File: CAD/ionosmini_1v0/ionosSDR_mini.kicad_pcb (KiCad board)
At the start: 4 copper layers, 168 x 80 mm, 63 parts, among them CON1 TFC-120-02-F-D-A-K-TR, CON2 TFC-120-02-F-D-A-K-TR, IC1 ESP32-S3-DEVKITC-1-N8R2, SW1 PTS647SK38SMTR2 LFS, SW2 PTS647SK38SMTR2 LFS, SW3 PTS647SK38SMTR2 LFS, SW4 PTS647SK38SMTR2 LFS, SW5 BACK, SW6 OK, U1 LP5907MFX-3.3

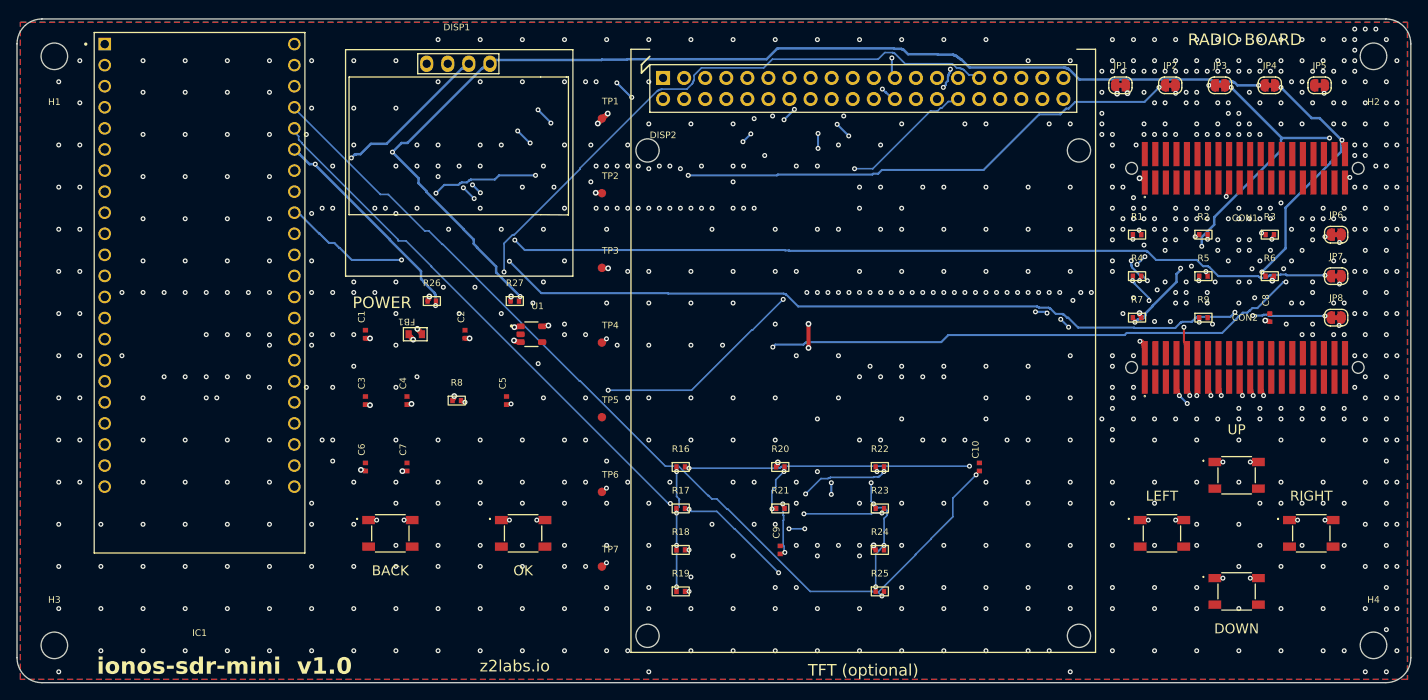
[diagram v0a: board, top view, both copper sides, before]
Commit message: rev-B3 PCB: pin map v2 parts, full re-route with 0/45/90 deg tracks
New parts placed: C11/C12 at the TFT VDD pin, R28-R32 header pull-ups
in a row under the display socket, R33 (NA 0R) and TP8 next to the
radio board sockets, R34 and the optional SW7 SPARE key.

All tracks and vias ripped and re-routed in three layer-role passes
(power on In2, the FG23 / TFT buses on In1, the rest on In1 and B.Cu;
F.Cu stays GND with pad fan-out only). Octilinear only: 0 % any-angle
segments, staircases straightened (1092 -> 970 segments), then GND
stitching on the new geometry (1394 vias, every GND island tied).

Silkscreen to JLCPCB rules (silk-to-pad 0.15 mm, line 0.15 mm, text
1.0/0.15 mm); references that sat on pads or on another part's silk
moved, FB1 turned upright, TP8 label pulled in from the board edge.
lib_footprint_mismatch warnings are expected: the board copies of
those footprints carry the trimmed silk.

TFC-120-02-F-D-A STEP replaced with the current Samtec model (same
geometry, AP214, coloured contacts); twin 3D reference images
recaptured, key still at the pin 1 end. DISP1 3D offset corrected.
twin_3d registers each 3D model's pins against its pads (steppins.py).

DRC 0 errors, 0 unconnected, schematic parity 0. README: buttons and
ladders, VRF_IN / 5V_RADIO, display and touch section, DevKit clone vs
official board note, new 3D render.
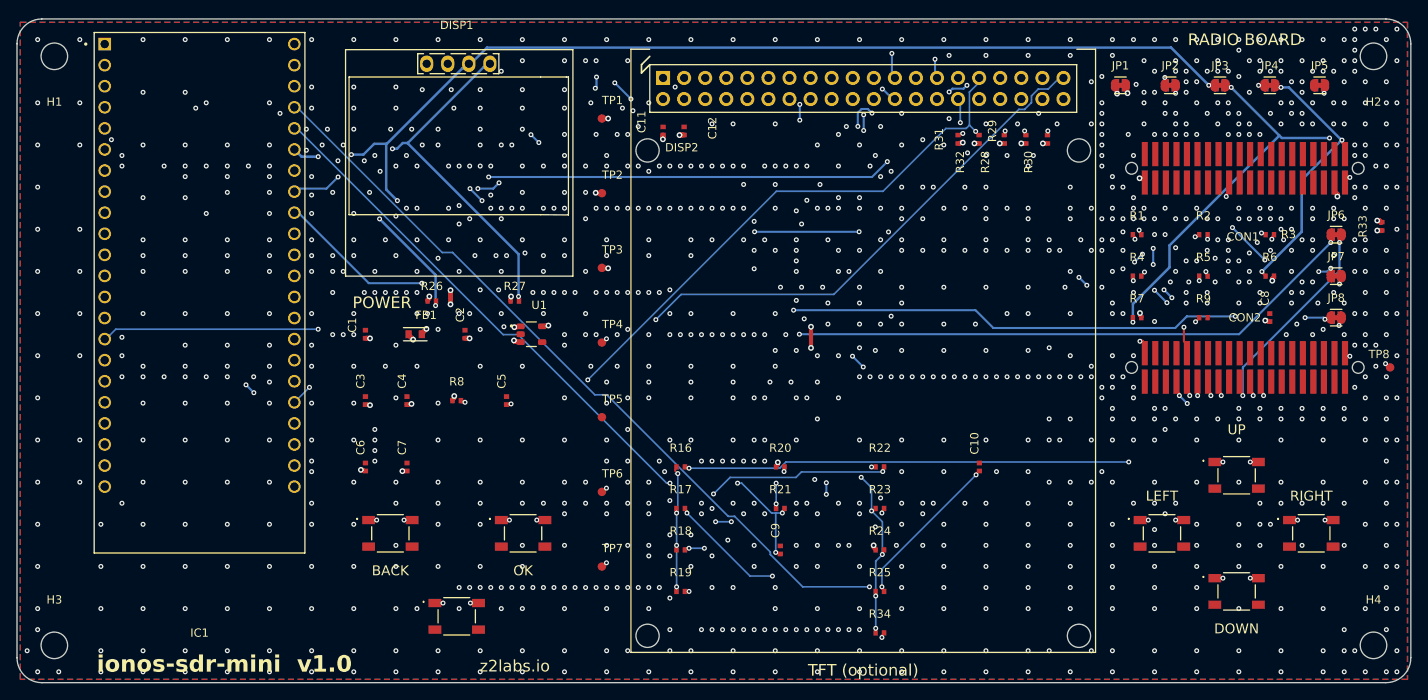
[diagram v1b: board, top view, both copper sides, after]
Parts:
- added C11: 10uF/6.3V, rpw_lib:CAPC1005X60_0402, F.Cu at (127.9, 63.5)
- added C12: 100nF/50V/10%, rpw_lib:CAPC1005X60_0402, F.Cu at (130.4, 63.5)
- added R28: 10k, rpw_lib:RESC1005X40_0402, F.Cu at (169.0, 64.5)
- added R29: 10k, rpw_lib:RESC1005X40_0402, F.Cu at (171.6, 64.5)
- added R30: 10k, rpw_lib:RESC1005X40_0402, F.Cu at (174.2, 64.5)
- added R31: 4.7k, rpw_lib:RESC1005X40_0402, F.Cu at (163.4, 64.5)
- added R32: 4.7k, rpw_lib:RESC1005X40_0402, F.Cu at (166.0, 64.5)
- added R33: NA(0R), rpw_lib:RESC1005X40_0402, F.Cu at (214.5, 75.0)
- added R34: 6.8k/1%, rpw_lib:RESC1005X40_0402, F.Cu at (154.0, 124.0)
- added SW7: NA(PTS647SK38), rpw_lib:PTS647SK38SMTR2LFS, F.Cu at (103.0, 122.0)
- added TP8: VRF_IN, rpw_lib:TESTPOINT_40MIL_SMD, F.Cu at (215.5, 92.0)
- C1, C6: value 10u -> 10uF/6.3V
- C10, C4, C5, C7, C8, C9: value 100n -> 100nF/50V/10%
- C2, C3: value 1u -> 1uF/16V/10%
- JP1, JP2, JP3, JP4, JP5, JP6, JP7, JP8: value ~ -> Bridged
- R17, R23: value 2k2 -> 2.2k/1%
- R18: value 6k8 -> 6.8k/1%
- R19: value 22k -> 22k/1%
- R20, R24: value 10k -> 10k/1%
- R26, R27: value 4k7 DNP -> NA(4.7k)
- SW5: value BACK -> PTS647SK38SMTR2 LFS
- SW6: value OK -> PTS647SK38SMTR2 LFS
- U1: value LP5907MFX-3.3 -> LP5907MFX-3.3(SOT23-5)
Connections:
- CON1 pad 37: unconnected-(CON1-Pad37) -> 5V_RADIO
- CON2 pad 40: unconnected-(CON2-Pad40) -> VRF_IN
- DISP2 pad 35: unconnected-(DISP2-SD_/CS-Pad35) -> SD_CS
- DISP2 pad 36: unconnected-(DISP2-FONT_/CS-Pad36) -> FONT_CS
- DISP2 pad 37: unconnected-(DISP2-FLASH_/CS-Pad37) -> FLASH_CS
- IC1 pad J1_15: TCH_B -> TCH_INT
- IC1 pad J3_18: TCH_INT -> TCH_B
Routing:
- net 5V0: track 98.6 -> 206.7 mm, vias 4 -> 8
- net BTN_A3: track 0.00 -> 57.2 mm, vias 0 -> 3
- net TCH_B: track 123.4 -> 103.1 mm, vias 1 -> 3
- net TCH_INT: track 109.2 -> 129.1 mm
- net 5V_RADIO: track 0.00 -> 8.46 mm, vias 0 -> 2
- net SD_CS: track 0.00 -> 7.73 mm, vias 0 -> 1
- net FLASH_CS: track 0.00 -> 7.63 mm, vias 0 -> 1
- net VRF_IN: track 0.00 -> 6.16 mm, vias 0 -> 2
- net BTN_A_RAW: track 18.4 -> 24.2 mm, vias 5 -> 6
- net TFT_CS: track 103.6 -> 109.4 mm, vias 1 -> 3
- net FONT_CS: track 0.00 -> 4.57 mm, vias 0 -> 1
- net TCH_A: track 111.6 -> 115.4 mm, vias 1 -> 2
- net FG23_CMD: track 98.1 -> 101.1 mm, vias 6 -> 7
- net TFT_DC: track 105.6 -> 107.2 mm, vias 2 -> 4
- net SWDIO: track 127.3 -> 128.8 mm, vias 2 -> 6
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
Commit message: PCB: stitch every GND pour pocket, centre tracks in their channels
The zone filler drops pieces of GND pour that have no connection
(island removal), so a strip of GND between two tracks with no via in
it was simply missing - white holes all over the 2-layer F.Cu. Every
such pocket now gets a via into connected GND on another layer
(0.45/0.3 mm where the 0.6/0.3 via does not fit), and the next fill
keeps it. What is left is narrower than a via, or has no connected
GND on any other layer to tie to (e.g. between the TFT header rows).

Straight runs that pass between obstacles on both sides (a track
between two header pins) are moved to the middle of the channel; the
neighbouring segments stay on their own lines, so the routing stays
0/45/90 deg.

DRC 0 errors, 0 unconnected, schematic parity 0; twin unchanged.
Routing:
- net 3V3_RADIO: track 171.4 -> 172.9 mm
- net TFT_SCK: track 116.2 -> 117.2 mm
- net FG23_RDY: track 95.5 -> 96.4 mm
- net TCH_INT: track 129.1 -> 129.8 mm
- net TFT_DC: track 107.2 -> 107.9 mm
- net TFT_CS: track 109.4 -> 109.9 mm
- net FG23_SPARE_RB: track 51.4 -> 51.9 mm
- net GND: vias 1193 -> 1283

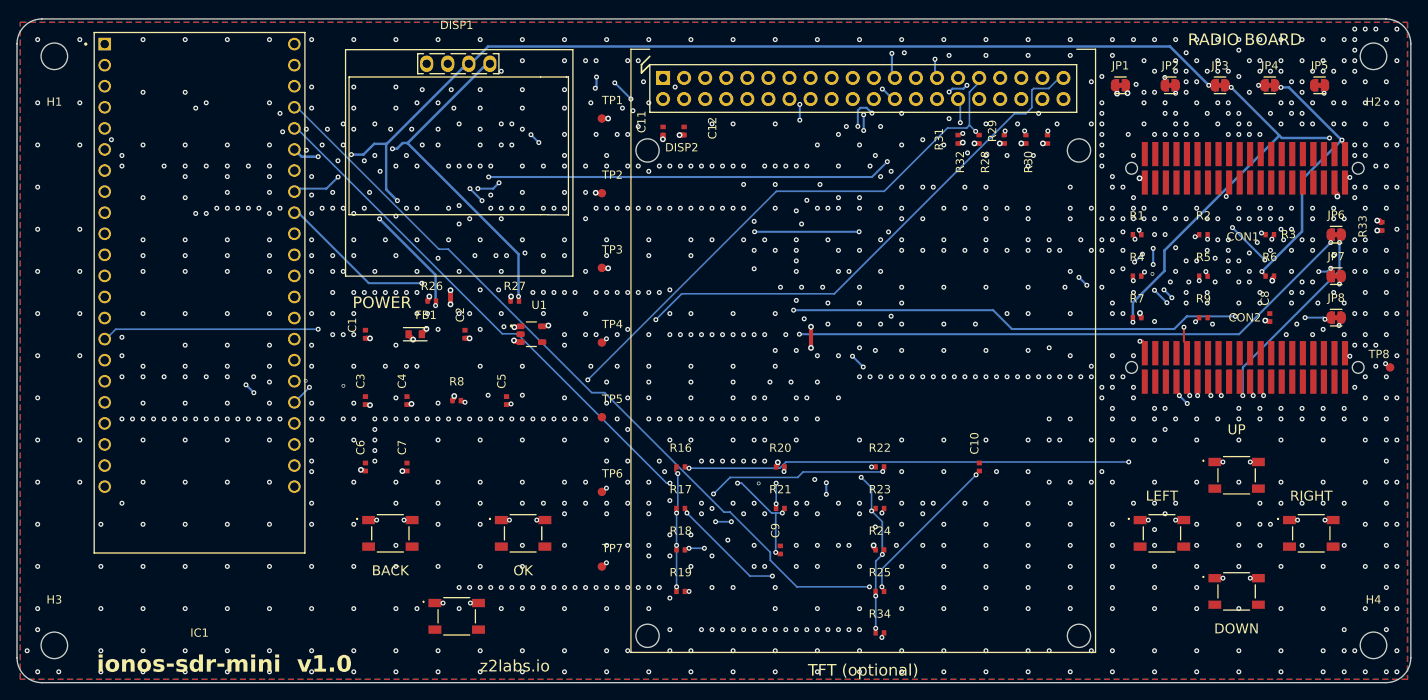
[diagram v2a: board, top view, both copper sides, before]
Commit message: SWD debug header CON3 (1x6 2.54 mm, not fitted) for an external debugger
Flashing the FG23 so far went only through the ESP32's bit-banged SWD.
CON3 adds a row of six plated holes on the right board edge, outside
the radio board's outline, for a J-Link / Simplicity Link with a pogo
clip or solder-in pins. Pin order follows the Tag-Connect TC2030-CTX:
1 VTref (VMCU_IN), 2 SWDIO, 3 nRESET, 4 SWCLK, 5 GND, 6 SWO.

The pins are on the radio side of the solder-jumper cut points
(SWDIO_RB, SWCLK_RB, SWO_RB, RESETn_RB): with JP2 and JP6-JP8 cut the
ESP32 is off the bus entirely; uncut, firmware keeps its SWD pins as
inputs while a debugger is attached. VTref only senses VMCU.

Schematic: radio sheet, new block with KiCad's TC2030 symbol (VCC top,
GND bottom) on a 1x6 header footprint; lint clean, ERC 0 errors.
twin_check asserts every CON3 pin reaches its radio-board pin.
twin_3d resolves KiCad's own ${KICADnn_3DMODEL_DIR} from the install.

PCB: TP8 moves 2 mm down to make room; full re-route (0/45/90),
GND pockets stitched, tracks centred in their channels. DRC 0 errors,
0 unconnected, schematic parity 0. 3D reference images recaptured
(CON3 and TP8 now beside CON2). README: SWD header section.
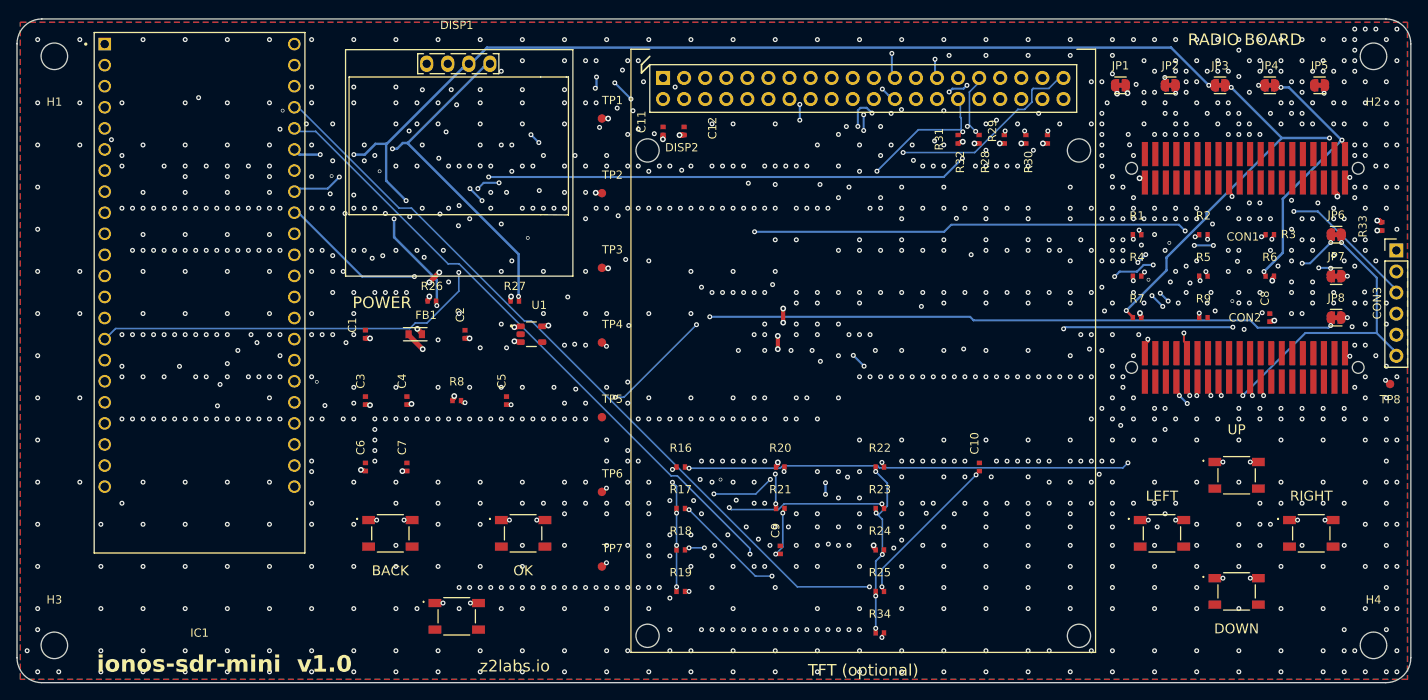
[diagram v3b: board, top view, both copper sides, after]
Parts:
- added CON3: NA(SWD 1x6 2.54), Connector_PinHeader_2.54mm:PinHeader_1x06_P2.54mm_Vertical, F.Cu at (216.2, 77.9)
- moved TP8 2.00 mm to (215.5, 94.0)
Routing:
- net VMCU_IN: track 88.5 -> 123.8 mm
- net RESETn_RB: track 17.8 -> 42.8 mm, vias 2 -> 3
- net 3V3: track 309.5 -> 291.4 mm, vias 16 -> 18
- net SWO_RB: track 26.2 -> 38.5 mm
- net 3V3_RADIO: track 172.9 -> 163.1 mm
- net SWDIO_RB: track 20.6 -> 27.8 mm
- net SWCLK_RB: track 15.5 -> 22.6 mm
- net FG23_MOSI: track 132.9 -> 137.8 mm
- net FG23_CMD: track 101.1 -> 99.0 mm
- net BTN_B: track 84.1 -> 86.2 mm, vias 4 -> 3
- net Net-(IC1B-GPIO14): track 146.4 -> 148.1 mm
- net TCH_INT: track 129.8 -> 131.4 mm
- net TFT_SCK: track 117.2 -> 118.5 mm
- net FG23_RDY: track 96.4 -> 95.1 mm
- net 5V_LDO: track 15.9 -> 16.8 mm
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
